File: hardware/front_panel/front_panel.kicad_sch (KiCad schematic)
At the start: 14 parts, among them J3 Display, J4 Main, SW1 Up, SW2 Down, SW3 Left, SW4 Rigth

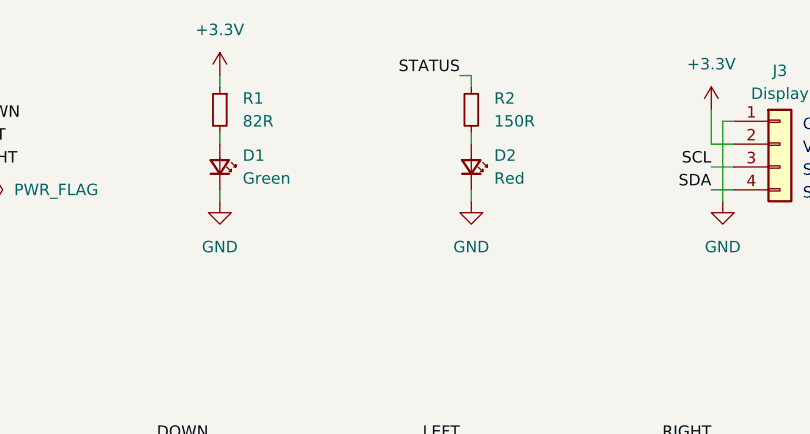
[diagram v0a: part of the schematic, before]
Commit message: Adjust component values
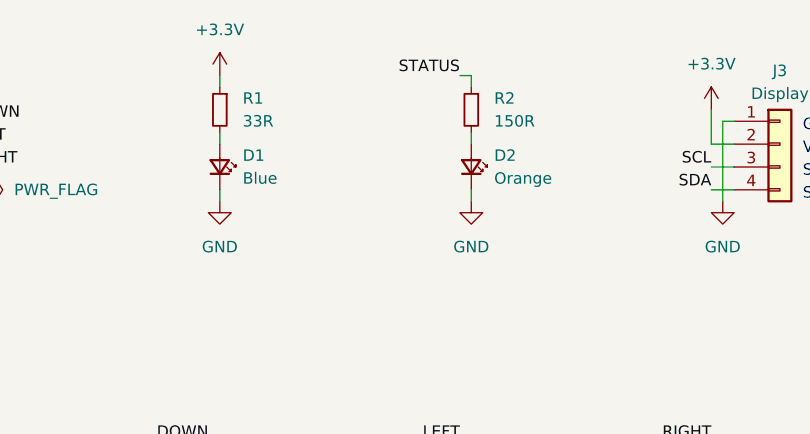
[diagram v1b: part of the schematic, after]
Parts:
- D1: value Green -> Blue
- D2: value Red -> Orange
- R1: value 82R -> 33R
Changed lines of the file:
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@@
       (effects (font (size 1.27 1.27)) (justify left))
     )
-    (property "Value" "Green" (at 138.43 76.2 90)
+    (property "Value" "Blue" (at 138.43 76.2 90)
       (effects (font (size 1.27 1.27)) (justify left))
     )
@@
       (effects (font (size 1.27 1.27)) (justify left))
     )
-    (property "Value" "Red" (at 166.37 76.2 90)
+    (property "Value" "Orange" (at 166.37 76.2 90)
       (effects (font (size 1.27 1.27)) (justify left))
     )
@@
       (effects (font (size 1.27 1.27)) (justify right))
     )
-    (property "Value" "82R" (at 138.43 69.85 0)
+    (property "Value" "33R" (at 138.43 69.85 0)
       (effects (font (size 1.27 1.27)) (justify right))
     )

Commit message: Assign footprints to components
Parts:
- removed J4: Main, Connector_PinHeader_2.54mm:PinHeader_2x05_P2.54mm_Vertical, symbol Connector_Generic:Conn_02x05_Top_Bottom
- added J1: Panel, Local_Library:52808-1070, symbol Connector_Generic:Conn_01x10
- D1: value Blue -> Green; Component (none) -> WP424GDT
- D2: Component (none) -> WP424EDT
- R1: value 33R -> 270R
- R2: value 150R -> 270R
- SW1, SW2, SW3: Component (none) -> PTS645SM702LFS
- SW4: value Rigth -> Right; Component (none) -> PTS645SM702LFS
- renumbered J3 to J2
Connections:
- net +3.3V: now also J1.10 (Pin_10)
- net DOWN: now also J1.4 (Pin_4)
- net GND: now also J1.1 (Pin_1), J1.7 (Pin_7)
- net LEFT: now also J1.3 (Pin_3)
- net RIGHT: now also J1.2 (Pin_2)
- net SCL: now also J1.9 (Pin_9)
- net SDA: now also J1.8 (Pin_8)
- net STATUS: now also J1.6 (Pin_6)
- net UP: now also J1.5 (Pin_5)
- no-connect marks 1 -> 0
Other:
- note added: "SCL"
- note added: "V_{F} = 2 V I_{F} = 10 mA"
- note removed: "SCK"

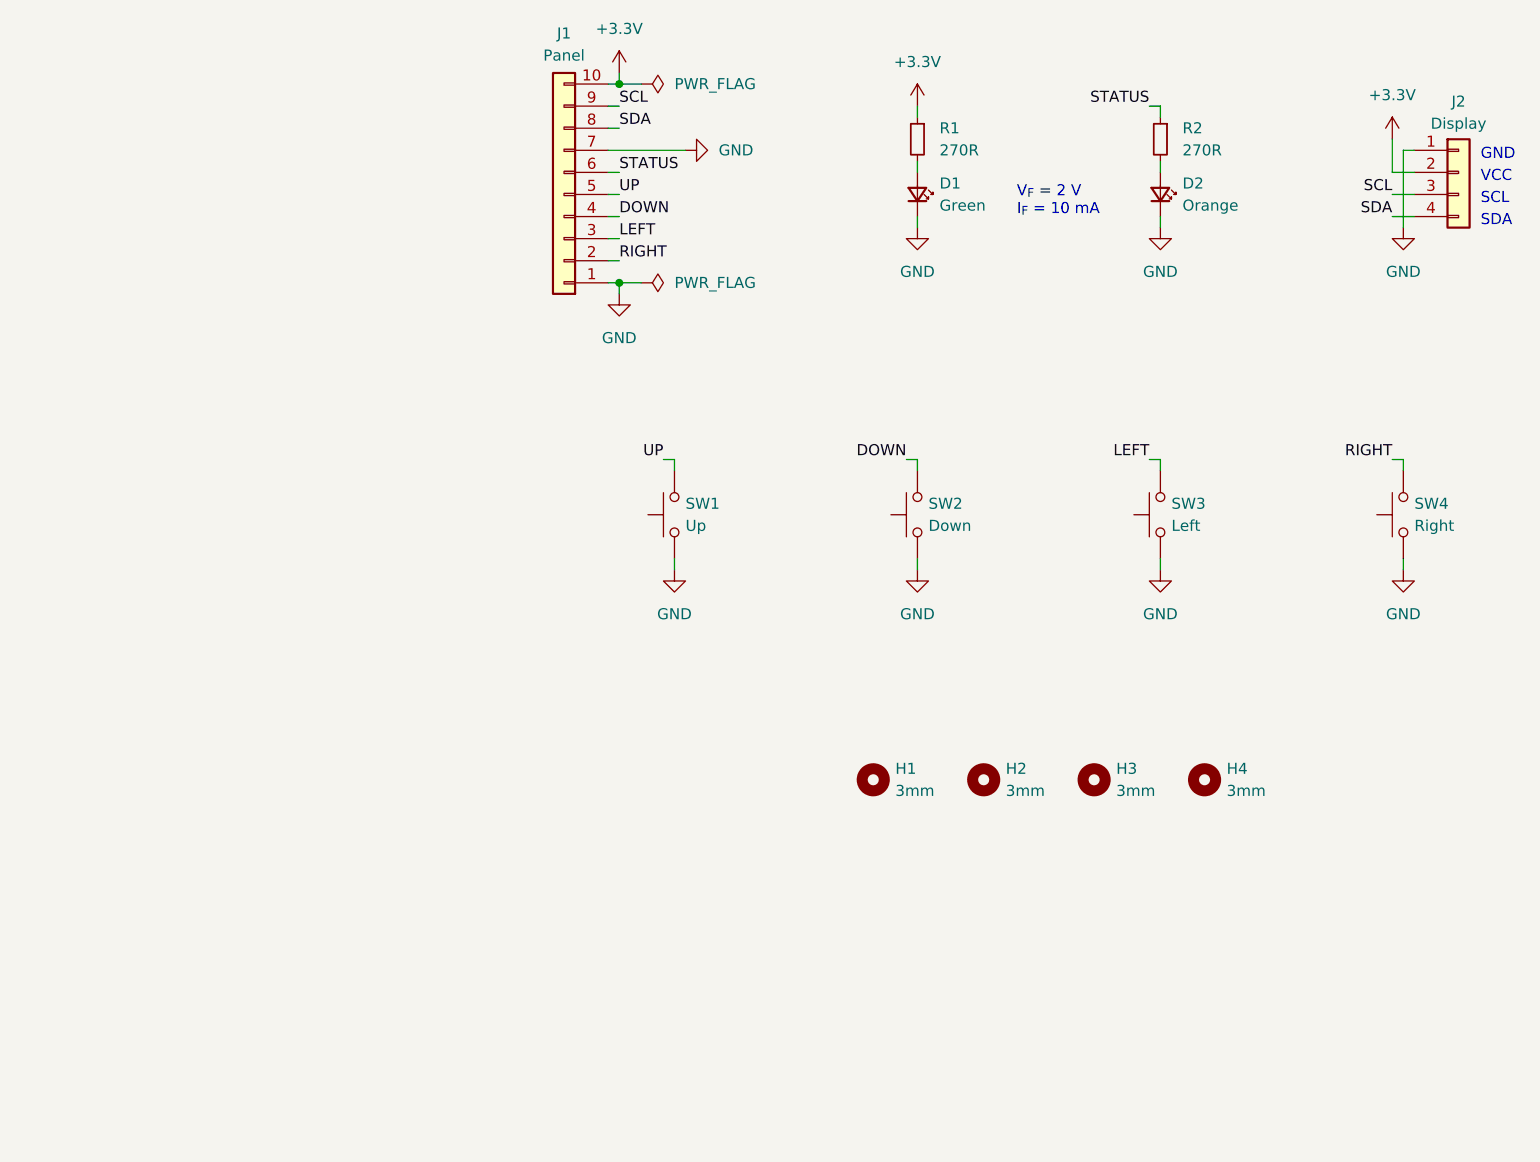
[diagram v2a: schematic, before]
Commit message: Place components on the front panel PCB
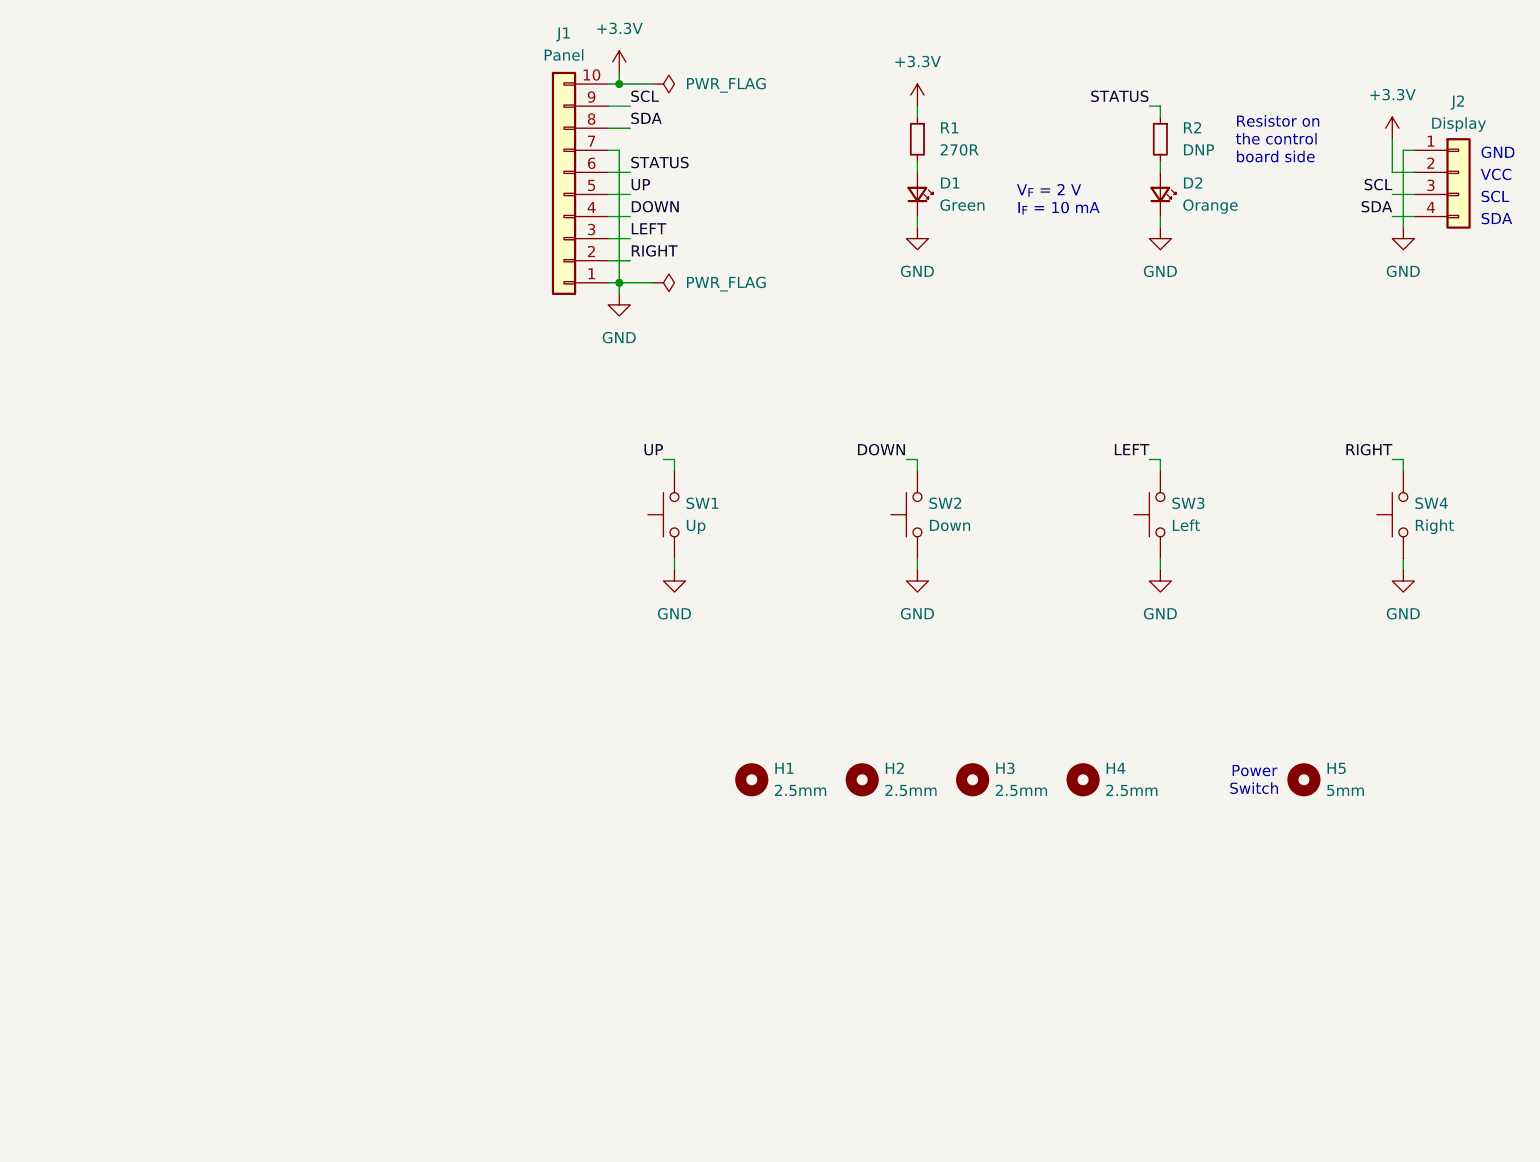
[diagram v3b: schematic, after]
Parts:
- added H5: 5mm, MountingHole:MountingHole_5mm, symbol Mechanical:MountingHole
- D1, D2: footprint LED_THT:LED_D3.0mm -> LED_THT:LED_D3.0mm_FlatTop
- H1, H2, H3, H4: value 3mm -> 2.5mm; footprint MountingHole:MountingHole_3mm -> MountingHole:MountingHole_2.5mm
- J2: footprint Connector_PinSocket_2.54mm:PinSocket_1x04_P2.54mm_Horizontal -> Connector_PinSocket_2.54mm:PinSocket_1x04_P2.54mm_Vertical
- R2: value 270R -> DNP; now left out of the parts list
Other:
- moved on the sheet: H1, H2, H3, H4

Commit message: Route front panel PCB tracks
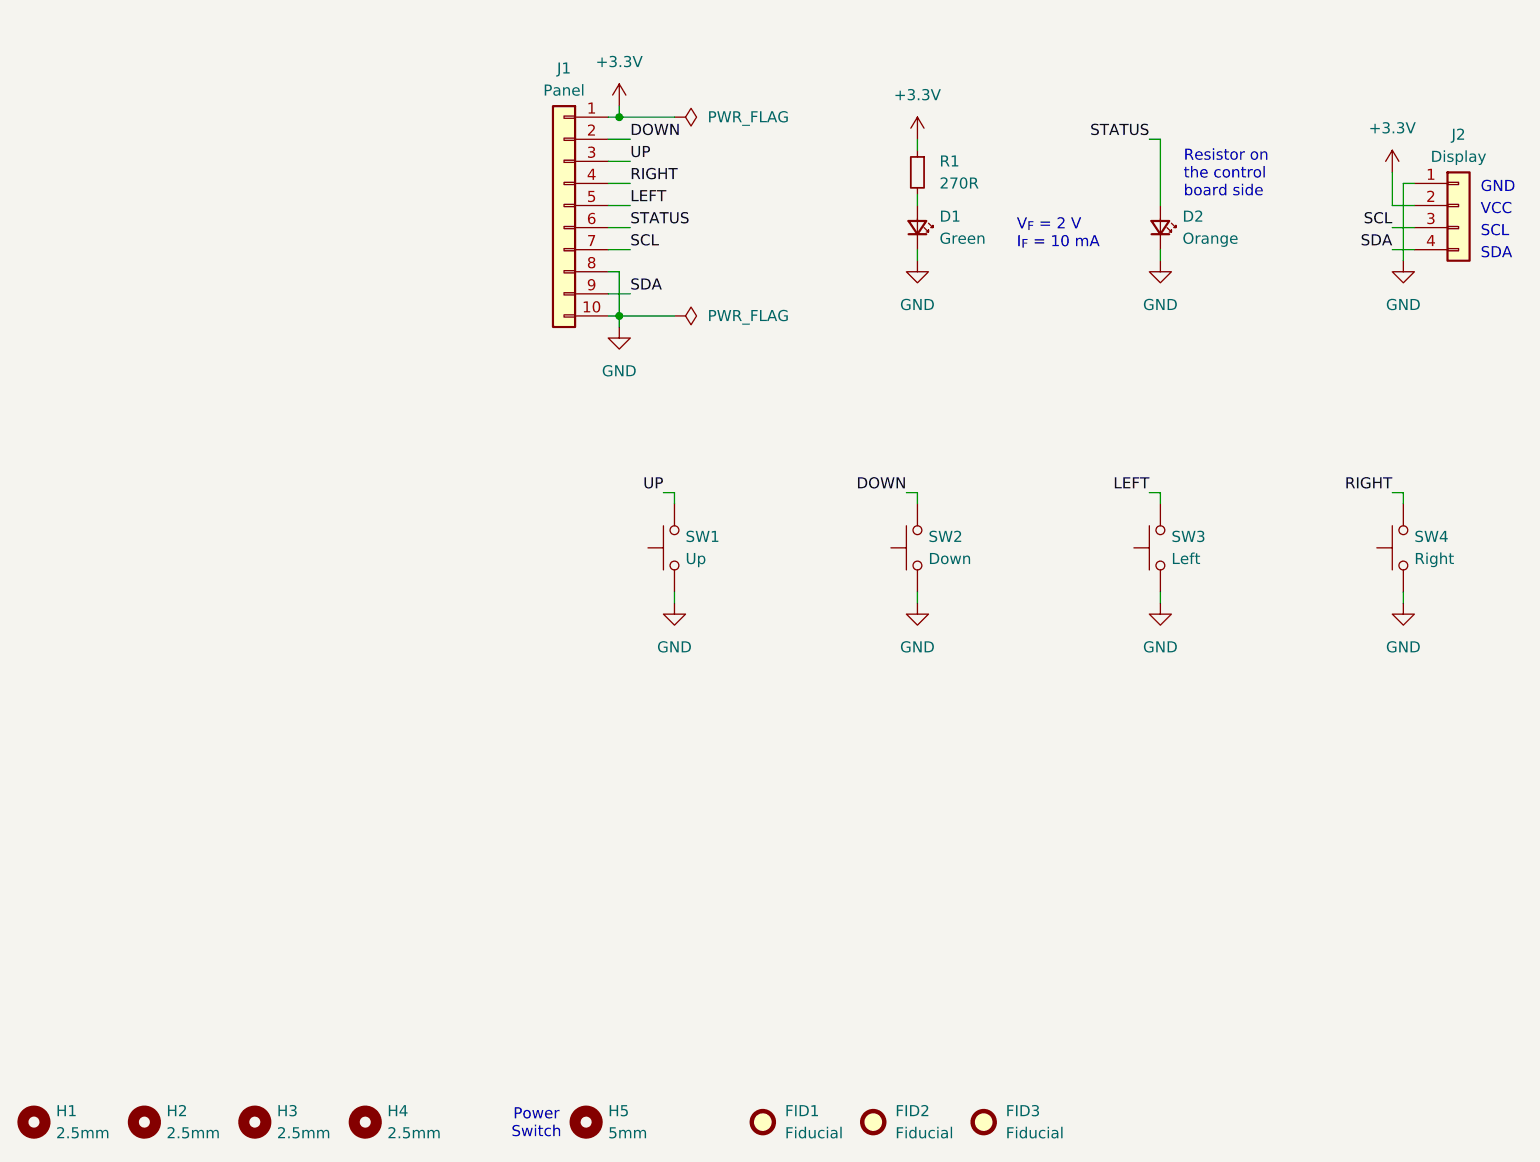
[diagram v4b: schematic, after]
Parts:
- removed R2: DNP, Resistor_SMD:R_0603_1608Metric, symbol Device:R_Small
- added FID1, FID2, FID3: Fiducial, Fiducial:Fiducial_1mm_Mask2mm, symbol Mechanical:Fiducial
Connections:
- net +3.3V: now also J1.1 (Pin_1); no longer J1.10 (Pin_10)
- net DOWN: now also J1.2 (Pin_2); no longer J1.4 (Pin_4)
- net GND: now also J1.10 (Pin_10), J1.8 (Pin_8); no longer J1.1 (Pin_1), J1.7 (Pin_7)
- net LEFT: now also J1.5 (Pin_5); no longer J1.3 (Pin_3)
- net RIGHT: now also J1.4 (Pin_4); no longer J1.2 (Pin_2)
- net SCL: now also J1.7 (Pin_7); no longer J1.9 (Pin_9)
- net SDA: now also J1.9 (Pin_9); no longer J1.8 (Pin_8)
- net STATUS: now also D2.2 (A)
- net UP: now also J1.3 (Pin_3); no longer J1.5 (Pin_5)
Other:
- moved on the sheet: D1, D2, H1, H2, H3, H4, H5, J1, J2, R1, SW1, SW2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

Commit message: Stitch the ground planes
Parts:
- J2: footprint Connector_PinSocket_2.54mm:PinSocket_1x04_P2.54mm_Vertical -> Local_Library:0.96_OLED
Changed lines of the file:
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@@
       (effects (font (size 1.27 1.27)) (justify top))
     )
-    (property "Footprint" "Connector_PinSocket_2.54mm:PinSocket_1x04_P2.54mm_Vertical" (at 198.12 76.2 0)
+    (property "Footprint" "Local_Library:0.96_OLED" (at 198.12 76.2 0)
       (effects (font (size 1.27 1.27)) hide)
     )
